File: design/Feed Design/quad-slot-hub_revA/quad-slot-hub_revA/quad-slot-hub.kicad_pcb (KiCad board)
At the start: 2 copper layers, 52 x 52 mm, 5 parts, among them J1 SMA_0732510250

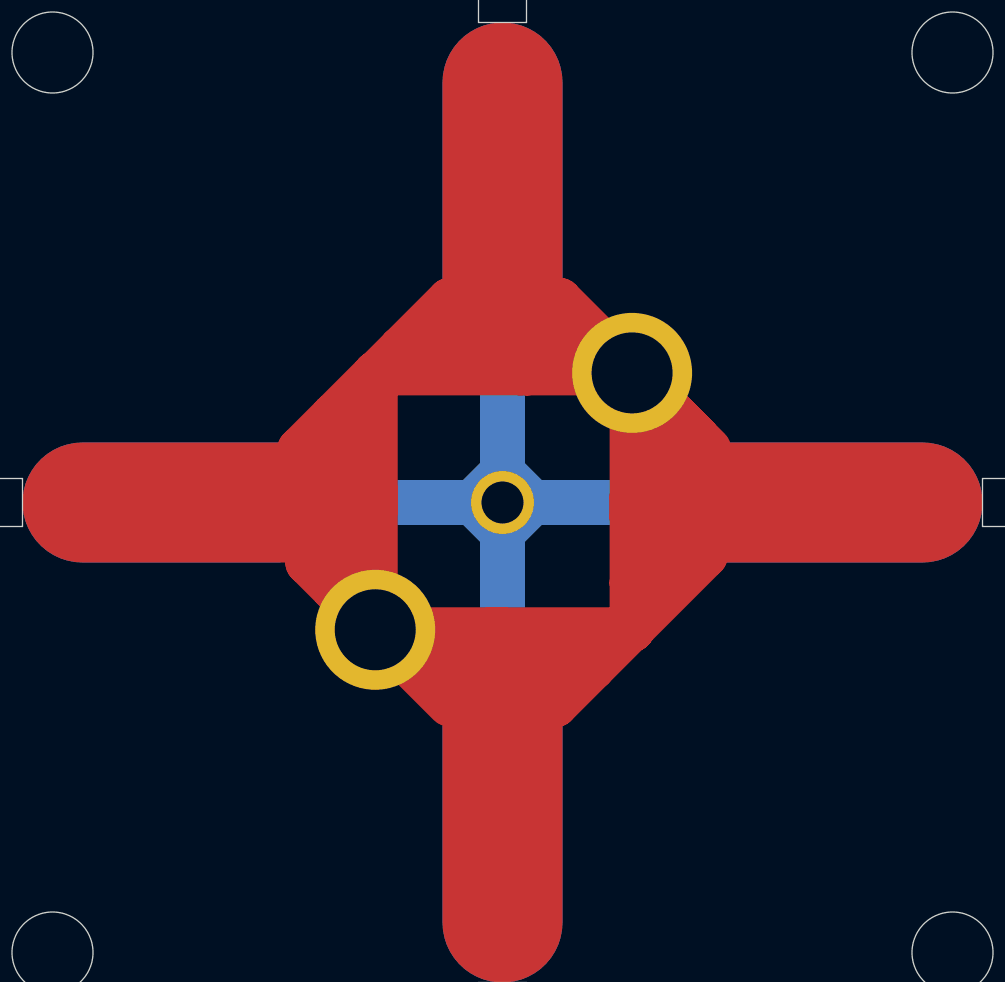
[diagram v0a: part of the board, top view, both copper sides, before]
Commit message: Updating trislots and other parts.
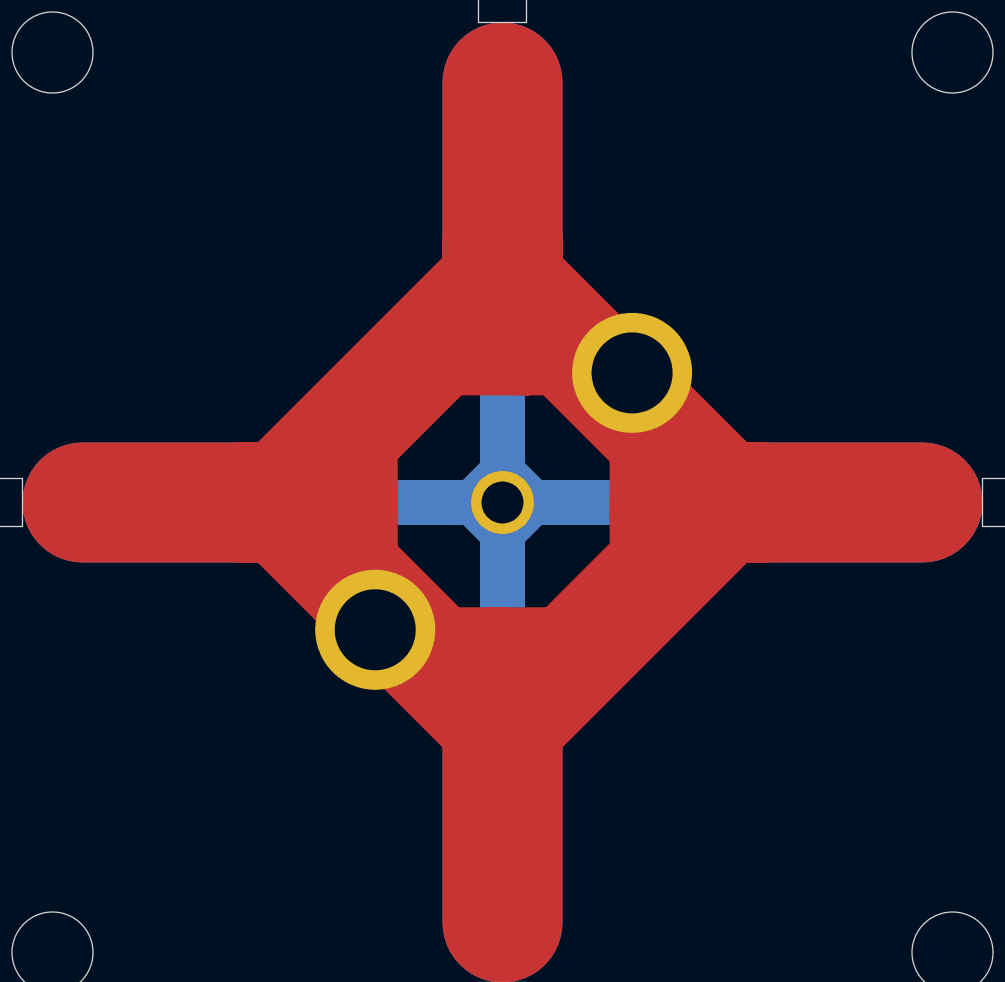
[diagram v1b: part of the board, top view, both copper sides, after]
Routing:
- net /slot_l: track 166.0 -> 255.9 mm
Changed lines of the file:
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@@
     (thickness 1.6)
     (drawings 18)
-    (tracks 124)
+    (tracks 136)
     (zones 0)
     (modules 5)
@@
   (page A4)
   (layers
-    (0 F.Cu signal hide)
+    (0 F.Cu signal)
     (31 B.Cu signal)
     (32 B.Adhes user)
@@
   )
   (setup
-    (last_trace_width 2)
+    (last_trace_width 0.5)
     (user_trace_width 0.5)
     (user_trace_width 1)
@@
       (effects (font (size 1 1) (thickness 0.15)))
     )
+    (fp_circle (center 0 0) (end 2.95 0) (layer F.CrtYd) (width 0.05))
     (fp_circle (center 0 0) (end 2.7 0) (layer Cmts.User) (width 0.15))
-    (fp_circle (center 0 0) (end 2.95 0) (layer F.CrtYd) (width 0.05))
     (fp_text user %R (at 0.3 0 90) (layer F.Fab)
       (effects (font (size 1 1) (thickness 0.15)))
@@
       (effects (font (size 1 1) (thickness 0.15)))
     )
+    (fp_circle (center 0 0) (end 2.95 0) (layer F.CrtYd) (width 0.05))
     (fp_circle (center 0 0) (end 2.7 0) (layer Cmts.User) (width 0.15))
-    (fp_circle (center 0 0) (end 2.95 0) (layer F.CrtYd) (width 0.05))
     (fp_text user %R (at 0.3 0) (layer F.Fab)
       (effects (font (size 1 1) (thickness 0.15)))
@@
       (effects (font (size 1 1) (thickness 0.15)))
     )
+    (fp_circle (center 0 0) (end 2.95 0) (layer F.CrtYd) (width 0.05))
     (fp_circle (center 0 0) (end 2.7 0) (layer Cmts.User) (width 0.15))
-    (fp_circle (center 0 0) (end 2.95 0) (layer F.CrtYd) (width 0.05))
     (fp_text user %R (at 0.3 0) (layer F.Fab)
       (effects (font (size 1 1) (thickness 0.15)))
@@
       (effects (font (size 1 1) (thickness 0.15)))
     )
+    (fp_circle (center 0 0) (end 2.95 0) (layer F.CrtYd) (width 0.05))
     (fp_circle (center 0 0) (end 2.7 0) (layer Cmts.User) (width 0.15))
-    (fp_circle (center 0 0) (end 2.95 0) (layer F.CrtYd) (width 0.05))
     (fp_text user %R (at 0.3 0) (layer F.Fab)
       (effects (font (size 1 1) (thickness 0.15)))
@@
   (segment (start -1.76001 -5.602351) (end -1.76001 -6.73999) (width 1.5) (layer F.Cu) (net 2))
   (segment (start -5.63501 -1.792669) (end -5.602351 -1.76001) (width 1.5) (layer F.Cu) (net 2))
-  (segment (start -5.63501 -2.88501) (end -5.63501 -1.792669) (width 1.5) (layer F.Cu) (net 2))
   (segment (start -5.63501 -2.88501) (end -6.76001 -1.76001) (width 1.5) (layer F.Cu) (net 2))
   (segment (start -4.242641 -4.277379) (end -5.63501 -2.88501) (width 1.5) (layer F.Cu) (net 2))
@@
   (segment (start 6.48999 -2.150854) (end 4.320422 -4.320422) (width 1.5) (layer F.Cu) (net 2))
   (segment (start 6.880834 -1.76001) (end 4.320422 -4.320422) (width 1.5) (layer F.Cu) (net 2))
-  (segment (start 4.320422 4.199598) (end 6.76001 1.76001) (width 1.5) (layer F.Cu) (net 2))
   (segment (start 4.320422 4.222578) (end 4.320422 4.199598) (width 1.5) (layer F.Cu) (net 2))
   (segment (start 5.602351 1.76001) (end 6.76001 1.76001) (width 1.5) (layer F.Cu) (net 2))
@@
   (segment (start 2.53999 5.03999) (end 3 5.5) (width 1.5) (layer F.Cu) (net 2))
   (segment (start 1.197649 5.03999) (end 2.53999 5.03999) (width 1.5) (layer F.Cu) (net 2))
-  (segment (start 4.257359 4.242641) (end 3 5.5) (width 1.5) (layer F.Cu) (net 2))
   (segment (start 3 5.5) (end 1.76001 6.73999) (width 1.5) (layer F.Cu) (net 2))
   (segment (start -3.527379 4.242641) (end -1.76001 6.01001) (width 1.5) (layer F.Cu) (net 2))
@@
   (segment (start 5.393544 -1.197649) (end 5.705905 -1.51001) (width 1) (layer F.Cu) (net 2))
   (segment (start 5.03999 -1.197649) (end 5.393544 -1.197649) (width 1) (layer F.Cu) (net 2))
-  (segment (start 6 0) (end 14 0) (width 4) (layer F.Cu) (net 2))
   (segment (start 4.320422 0.124527) (end 5.705905 1.51001) (width 1) (layer F.Cu) (net 2))
-  (segment (start 4.320422 0.478422) (end 4.320422 2.679578) (width 1.5) (layer F.Cu) (net 2))
   (segment (start 4.320422 0.478422) (end 4.320422 0.124527) (width 1) (layer F.Cu) (net 2))
   (segment (start 4.320422 -0.179578) (end 4.320422 0.478422) (width 1.5) (layer F.Cu) (net 2))
@@
   (segment (start 0.604578 -4.320422) (end 0.820422 -4.320422) (width 1.5) (layer F.Cu) (net 2))
   (segment (start -4.20086 -4.320422) (end 0.604578 -4.320422) (width 1.5) (layer F.Cu) (net 2))
-  (segment (start 0 -6) (end 0 -14) (width 4) (layer F.Cu) (net 2))
   (segment (start -5.03999 0.33701) (end -5.03999 0.844095) (width 1) (layer F.Cu) (net 2))
   (segment (start -5.03999 0.844095) (end -5.705905 1.51001) (width 1) (layer F.Cu) (net 2))
@@
   (segment (start -0.844095 5.03999) (end -1.51001 5.705905) (width 1) (layer F.Cu) (net 2))
   (segment (start 0.12299 5.03999) (end -0.844095 5.03999) (width 1) (layer F.Cu) (net 2))
+  (segment (start 0 6) (end -6 0) (width 1.5) (layer F.Cu) (net 2))
+  (segment (start -6 0) (end 0 -6) (width 1.5) (layer F.Cu) (net 2))
+  (segment (start 0 -6) (end 6 0) (width 1.5) (layer F.Cu) (net 2))
+  (segment (start 6 0) (end 0 6) (width 1.5) (layer F.Cu) (net 2))
+  (segment (start -0.75 8) (end -8.75 0) (width 2) (layer F.Cu) (net 2))
+  (segment (start 0 8) (end -0.75 8) (width 2) (layer F.Cu) (net 2))
+  (segment (start 0 6) (end 0 8) (width 4) (layer F.Cu) (net 2))
   (segment (start 0 6) (end 0 14) (width 4) (layer F.Cu) (net 2))
+  (segment (start -6 0) (end -8.75 0) (width 4) (layer F.Cu) (net 2))
   (segment (start -6 0) (end -14 0) (width 4) (layer F.Cu) (net 2))
+  (segment (start -8.75 0) (end 0 -8.75) (width 2) (layer F.Cu) (net 2))
+  (segment (start 0 -6) (end 0 -8.75) (width 4) (layer F.Cu) (net 2))
+  (segment (start 0 -6) (end 0 -14) (width 4) (layer F.Cu) (net 2))
+  (segment (start 0 -8.75) (end 8.75 0) (width 2) (layer F.Cu) (net 2))
+  (segment (start 6 0) (end 8.75 0) (width 4) (layer F.Cu) (net 2))
+  (segment (start 6 0) (end 14 0) (width 4) (layer F.Cu) (net 2))
+  (segment (start 0 8.75) (end 8.75 0) (width 2) (layer F.Cu) (net 2))
+  (segment (start 4.320422 0.478422) (end 4.320422 2.679578) (width 1.5) (layer F.Cu) (net 2))
+  (segment (start -5.63501 -2.88501) (end -5.63501 -1.792669) (width 1.5) (layer F.Cu) (net 2))
+  (segment (start 4.257359 4.242641) (end 3 5.5) (width 1.5) (layer F.Cu) (net 2))
 )
